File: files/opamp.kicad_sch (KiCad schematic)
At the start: 1 part, among them U1 TL072

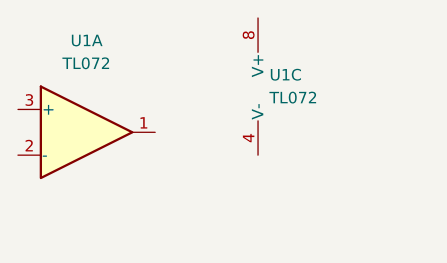
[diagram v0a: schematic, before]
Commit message: handle shape size without graphic items
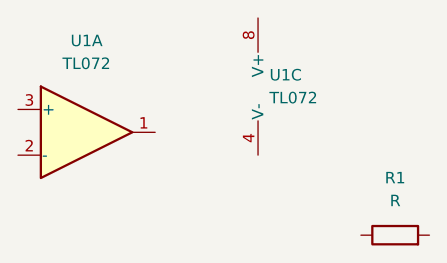
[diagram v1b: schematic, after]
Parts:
- added R1: R, symbol Device:R
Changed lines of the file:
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@@
     (pin "8")
+  )
+  (symbol (lib_id "Device:R") (at 88.9 50.8 90) (unit 1)
+    (in_bom yes) (on_board yes) (fields_autoplaced)
+    (property "Reference" "R1" (id 0) (at 88.9 44.45 90))
+    (property "Value" "R" (id 1) (at 88.9 46.99 90))
+    (property "Footprint" "" (id 2) (at 88.9 52.578 90)
+      (effects (font (size 1.27 1.27)) hide)
+    )
+    (property "Datasheet" "~" (id 3) (at 88.9 50.8 0)
+      (effects (font (size 1.27 1.27)) hide)
+    )
+    (pin "1")
+    (pin "2")
   )
   (sheet_instances
@@
   )
   (symbol_instances
+    (path "/c702b049-c387-4d28-a23a-3e9ed6315ee5"
+      (reference "R1") (unit 1) (value "R") (footprint "")
+    )
     (path "/5368d4f7-087e-45c1-8f28-463f84894808"
       (reference "U1") (unit 1) (value "TL072") (footprint "")
